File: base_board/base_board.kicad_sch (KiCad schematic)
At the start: 56 parts, among them J1 Conn_ARM_JTAG_SWD_20, SW1 SW_Push, U1 STM32F446ZEJx, U2 IS42S16400J-xT, U3 BMI270, U4 USB_C_Receptacle_USB2.0, U5 10p, U6 10p, U7 LD3985M33R_SOT23, Y1 Crystal_GND24

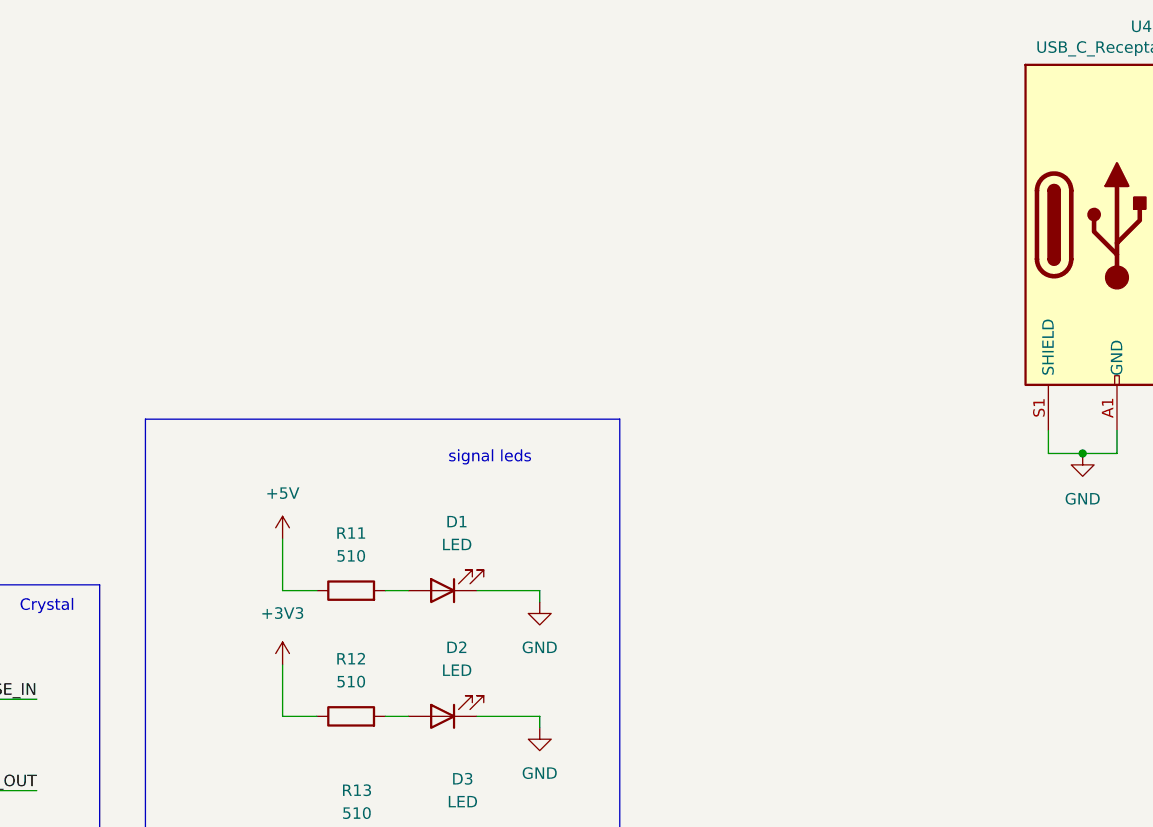
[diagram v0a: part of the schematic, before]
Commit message: [pcb] added onboard uart
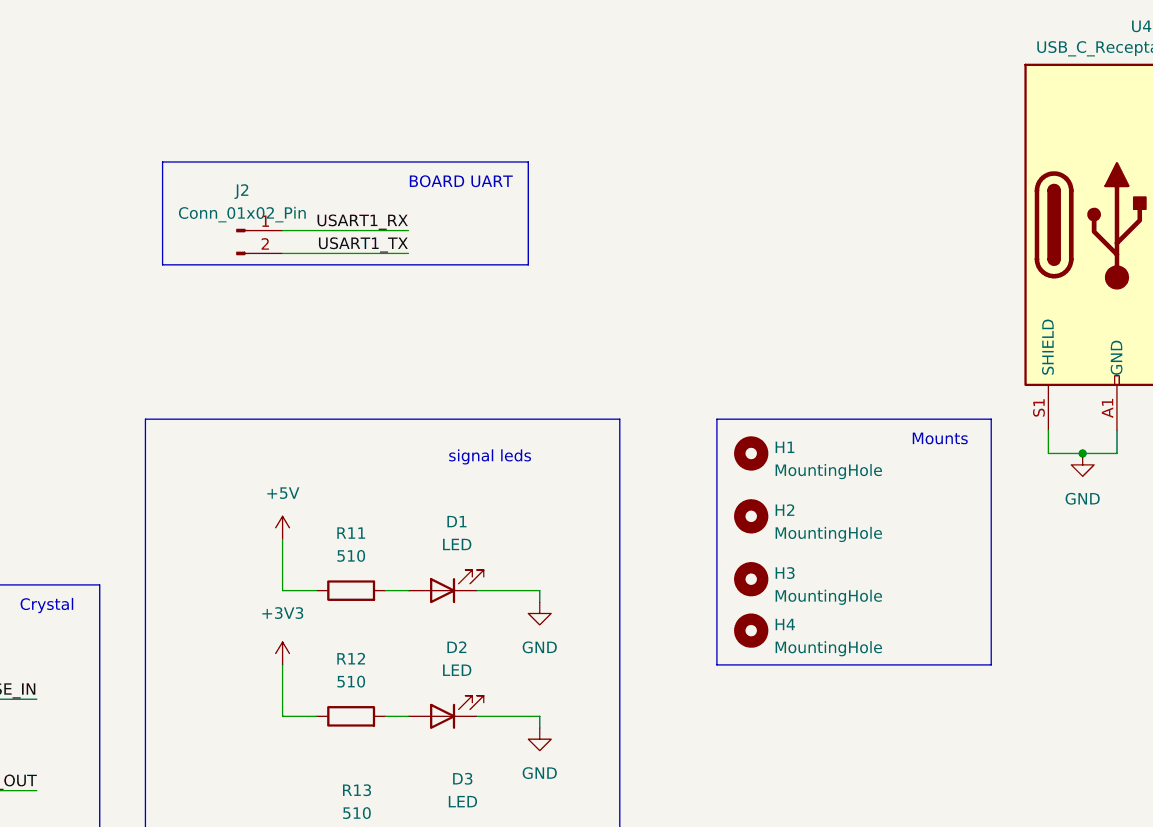
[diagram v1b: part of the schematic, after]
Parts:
- added H1, H2, H3, H4: MountingHole, MountingHole:MountingHole_3.2mm_M3, symbol Mechanical:MountingHole
- added J2: Conn_01x02_Pin, Connector_PinHeader_2.54mm:PinHeader_1x02_P2.54mm_Vertical, symbol Connector:Conn_01x02_Pin
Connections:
- net USART1_RX: now also J2.1 (Pin_1)
- net USART1_TX: now also J2.2 (Pin_2)
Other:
- note added: "BOARD UART"
- note added: "Mounts"
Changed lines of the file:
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@@
+    (stroke (width 0) (type default))
+  )
+  (wire (pts (xy 250.19 206.375) (xy 264.16 206.375))
     (stroke (width 0) (type default))
   )
@@
     (stroke (width 0) (type default))
   )
+  (wire (pts (xy 250.19 203.835) (xy 264.16 203.835))
+    (stroke (width 0) (type default))
+  )
   (wire (pts (xy 257.81 54.61) (xy 275.59 54.61))
     (stroke (width 0) (type default))
@@
     (stroke (width 0) (type default))
   )
+  (rectangle (start 236.855 196.215) (end 277.495 207.645)
+    (stroke (width 0) (type default))
+    (fill (type none))
+  )
+  (rectangle (start 298.45 224.79) (end 328.93 252.095)
+    (stroke (width 0) (type default))
+    (fill (type none))
+  )
   (text "JTAG" (at 86.995 17.78 0)
     (effects (font (size 1.27 1.27)) (justify left bottom))
   )
+  (text "BOARD UART\n" (at 264.16 199.39 0)
+    (effects (font (size 1.27 1.27)) (justify left bottom))
+  )
   (text "Reset circuit" (at 70.485 246.38 0)
     (effects (font (size 1.27 1.27)) (justify left bottom))
@@
     (effects (font (size 1.27 1.27)) (justify left bottom))
   )
+  (text "Mounts\n" (at 320.04 227.965 0)
+    (effects (font (size 1.27 1.27)) (justify left bottom))
+  )
   (text "imu sensor" (at 97.155 107.95 0)
     (effects (font (size 1.27 1.27)) (justify left bottom))
@@
     (effects (font (size 1.27 1.27)) (justify right bottom))
   )
+  (label "USART1_TX" (at 264.16 206.375 180) (fields_autoplaced)
+    (effects (font (size 1.27 1.27)) (justify right bottom))
+  )
   (label "FMC_A8" (at 257.81 82.55 0) (fields_autoplaced)
     (effects (font (size 1.27 1.27)) (justify left bottom))
@@
   (label "PF7" (at 123.19 134.62 0) (fields_autoplaced)
     (effects (font (size 1.27 1.27)) (justify left bottom))
+  )
+  (label "USART1_RX" (at 264.16 203.835 180) (fields_autoplaced)
+    (effects (font (size 1.27 1.27)) (justify right bottom))
   )
   (label "FMC_SDNE1" (at 222.25 88.9 180) (fields_autoplaced)
@@
         (path "/2307506f-1d7e-4fdb-b101-b9905788fe29"
           (reference "J1") (unit 1)
+        )
+      )
+    )
+  )
+  (symbol (lib_id "Mechanical:MountingHole") (at 302.26 248.285 0) (unit 1)
+    (in_bom yes) (on_board yes) (dnp no) (fields_autoplaced)
+    (property "Reference" "H4" (at 304.8 247.65 0)
+      (effects (font (size 1.27 1.27)) (justify left))
+    )
+    (property "Value" "MountingHole" (at 304.8 250.19 0)
+      (effects (font (size 1.27 1.27)) (justify left))
+    )
+    (property "Footprint" "MountingHole:MountingHole_3.2mm_M3" (at 302.26 248.285 0)
+      (effects (font (size 1.27 1.27)) hide)
+    )
+    (property "Datasheet" "~" (at 302.26 248.285 0)
+      (effects (font (size 1.27 1.27)) hide)
+    )
+    (instances
+      (project "base_board"
+        (path "/2307506f-1d7e-4fdb-b101-b9905788fe29"
+          (reference "H4") (unit 1)
         )
       )
@@
     )
   )
+  (symbol (lib_id "Connector:Conn_01x02_Pin") (at 245.11 203.835 0) (unit 1)
+    (in_bom yes) (on_board yes) (dnp no) (fields_autoplaced)
+    (property "Reference" "J2" (at 245.745 199.39 0)
+      (effects (font (size 1.27 1.27)))
+    )
+    (property "Value" "Conn_01x02_Pin" (at 245.745 201.93 0)
+      (effects (font (size 1.27 1.27)))
+    )
+    (property "Footprint" "Connector_PinHeader_2.54mm:PinHeader_1x02_P2.54mm_Vertical" (at 245.11 203.835 0)
+      (effects (font (size 1.27 1.27)) hide)
+    )
+    (property "Datasheet" "~" (at 245.11 203.835 0)
+      (effects (font (size 1.27 1.27)) hide)
+    )
+    (pin "1")
+    (pin "2")
+    (instances
+      (project "base_board"
+        (path "/2307506f-1d7e-4fdb-b101-b9905788fe29"
+          (reference "J2") (unit 1)
+        )
+      )
+    )
+  )
   (symbol (lib_id "power:+3V3") (at 92.075 122.555 0) (unit 1)
     (in_bom yes) (on_board yes) (dnp no) (fields_autoplaced)
@@
         (path "/2307506f-1d7e-4fdb-b101-b9905788fe29"
           (reference "R7") (unit 1)
+        )
+      )
+    )
+  )
+  (symbol (lib_id "Mechanical:MountingHole") (at 302.26 228.6 0) (unit 1)
+    (in_bom yes) (on_board yes) (dnp no) (fields_autoplaced)
+    (property "Reference" "H1" (at 304.8 227.965 0)
+      (effects (font (size 1.27 1.27)) (justify left))
+    )
+    (property "Value" "MountingHole" (at 304.8 230.505 0)
+      (effects (font (size 1.27 1.27)) (justify left))
+    )
+    (property "Footprint" "MountingHole:MountingHole_3.2mm_M3" (at 302.26 228.6 0)
+      (effects (font (size 1.27 1.27)) hide)
+    )
+    (property "Datasheet" "~" (at 302.26 228.6 0)
+      (effects (font (size 1.27 1.27)) hide)
+    )
+    (instances
+      (project "base_board"
+        (path "/2307506f-1d7e-4fdb-b101-b9905788fe29"
+          (reference "H1") (unit 1)
         )
       )
@@
     )
   )
+  (symbol (lib_id "Mechanical:MountingHole") (at 302.26 242.57 0) (unit 1)
+    (in_bom yes) (on_board yes) (dnp no) (fields_autoplaced)
+    (property "Reference" "H3" (at 304.8 241.935 0)
+      (effects (font (size 1.27 1.27)) (justify left))
+    )
+    (property "Value" "MountingHole" (at 304.8 244.475 0)
+      (effects (font (size 1.27 1.27)) (justify left))
+    )
+    (property "Footprint" "MountingHole:MountingHole_3.2mm_M3" (at 302.26 242.57 0)
+      (effects (font (size 1.27 1.27)) hide)
+    )
+    (property "Datasheet" "~" (at 302.26 242.57 0)
+      (effects (font (size 1.27 1.27)) hide)
+    )
+    (instances
+      (project "base_board"
+        (path "/2307506f-1d7e-4fdb-b101-b9905788fe29"
+          (reference "H3") (unit 1)
+        )
+      )
+    )
+  )
   (symbol (lib_id "Device:C") (at 323.85 154.94 0) (unit 1)
     (in_bom yes) (on_board yes) (dnp no) (fields_autoplaced)
@@
         )
       )
+    )
+  )
+  (symbol (lib_id "Mechanical:MountingHole") (at 302.26 235.585 0) (unit 1)
+    (in_bom yes) (on_board yes) (dnp no) (fields_autoplaced)
+    (property "Reference" "H2" (at 304.8 234.95 0)
+      (effects (font (size 1.27 1.27)) (justify left))
+    )
+    (property "Value" "MountingHole" (at 304.8 237.49 0)
+      (effects (font (size 1.27 1.27)) (justify left))
+    )
+    (property "Footprint" "MountingHole:MountingHole_3.2mm_M3" (at 302.26 235.585 0)
+      (effects (font (size 1.27 1.27)) hide)
+    )
+    (property "Datasheet" "~" (at 302.26 235.585 0)
+      (effects (font (size 1.27 1.27)) hide)
+    )
+    (instances
+      (project "base_board"
+        (path "/2307506f-1d7e-4fdb-b101-b9905788fe29"
+          (reference "H2") (unit 1)
+        )
+      )

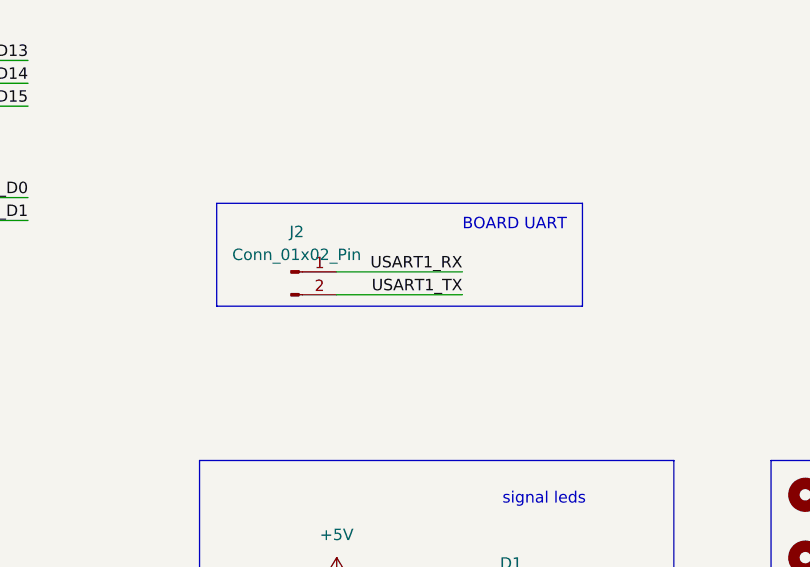
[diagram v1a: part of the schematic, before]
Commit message: [pcb] added gnd+3v3 for uart socket
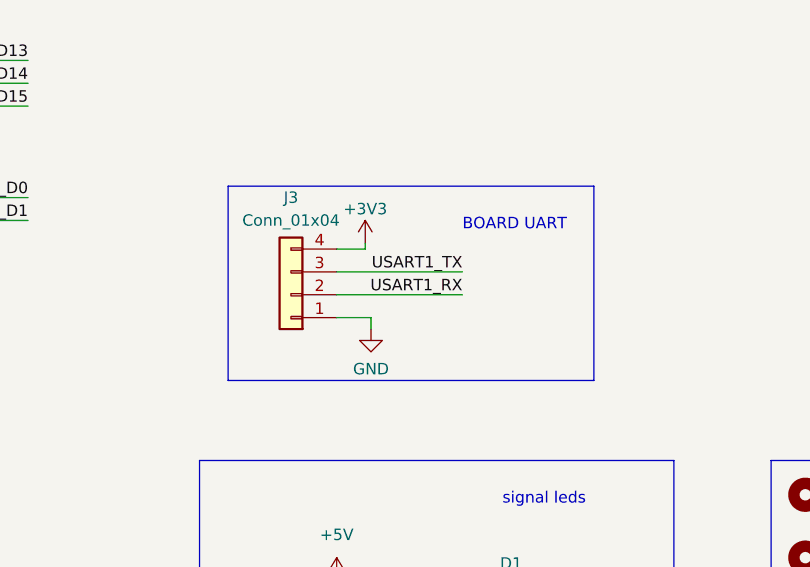
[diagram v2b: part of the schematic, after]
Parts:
- removed J2: Conn_01x02_Pin, Connector_PinHeader_2.54mm:PinHeader_1x02_P2.54mm_Vertical, symbol Connector:Conn_01x02_Pin
- added J3: Conn_01x04, Connector_PinHeader_2.54mm:PinHeader_1x04_P2.54mm_Vertical, symbol Connector_Generic:Conn_01x04
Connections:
- net +3V3: now also J3.4 (Pin_4)
- net GND: now also J3.1 (Pin_1)
- net USART1_RX: now also J3.2 (Pin_2)
- net USART1_TX: now also J3.3 (Pin_3)
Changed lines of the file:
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@@
+    (stroke (width 0) (type default))
+  )
+  (wire (pts (xy 253.365 200.66) (xy 253.365 201.295))
     (stroke (width 0) (type default))
   )
@@
     (stroke (width 0) (type default))
   )
+  (wire (pts (xy 253.365 201.295) (xy 250.19 201.295))
+    (stroke (width 0) (type default))
+  )
   (polyline (pts (xy 234.95 280.035) (xy 287.655 280.035))
     (stroke (width 0) (type default))
@@
     (stroke (width 0) (type default))
   )
+  (wire (pts (xy 254 208.915) (xy 250.19 208.915))
+    (stroke (width 0) (type default))
+  )
   (wire (pts (xy 123.825 73.66) (xy 138.43 73.66))
     (stroke (width 0) (type default))
@@
     (stroke (width 0) (type default))
   )
+  (wire (pts (xy 254 210.185) (xy 254 208.915))
+    (stroke (width 0) (type default))
+  )
   (wire (pts (xy 300.99 54.61) (xy 311.15 54.61))
     (stroke (width 0) (type default))
@@
     (stroke (width 0) (type default))
   )
-  (rectangle (start 236.855 196.215) (end 277.495 207.645)
+  (rectangle (start 238.125 194.31) (end 278.765 215.9)
     (stroke (width 0) (type default))
     (fill (type none))
@@
     (effects (font (size 1.27 1.27)) (justify right bottom))
   )
-  (label "USART1_TX" (at 264.16 206.375 180) (fields_autoplaced)
+  (label "USART1_TX" (at 264.16 203.835 180) (fields_autoplaced)
     (effects (font (size 1.27 1.27)) (justify right bottom))
   )
@@
     (effects (font (size 1.27 1.27)) (justify left bottom))
   )
-  (label "USART1_RX" (at 264.16 203.835 180) (fields_autoplaced)
+  (label "USART1_RX" (at 264.16 206.375 180) (fields_autoplaced)
     (effects (font (size 1.27 1.27)) (justify right bottom))
   )
@@
         (path "/2307506f-1d7e-4fdb-b101-b9905788fe29"
           (reference "R1") (unit 1)
+        )
+      )
+    )
+  )
+  (symbol (lib_name "+3V3_8") (lib_id "power:+3V3") (at 253.365 200.66 0) (unit 1)
+    (in_bom yes) (on_board yes) (dnp no) (fields_autoplaced)
+    (property "Reference" "#PWR011" (at 253.365 204.47 0)
+      (effects (font (size 1.27 1.27)) hide)
+    )
+    (property "Value" "+3V3" (at 253.365 196.85 0)
+      (effects (font (size 1.27 1.27)))
+    )
+    (property "Footprint" "" (at 253.365 200.66 0)
+      (effects (font (size 1.27 1.27)) hide)
+    )
+    (property "Datasheet" "" (at 253.365 200.66 0)
+      (effects (font (size 1.27 1.27)) hide)
+    )
+    (pin "1")
+    (instances
+      (project "base_board"
+        (path "/2307506f-1d7e-4fdb-b101-b9905788fe29"
+          (reference "#PWR011") (unit 1)
         )
       )
@@
     )
   )
-  (symbol (lib_id "Connector:Conn_01x02_Pin") (at 245.11 203.835 0) (unit 1)
-    (in_bom yes) (on_board yes) (dnp no) (fields_autoplaced)
-    (property "Reference" "J2" (at 245.745 199.39 0)
-      (effects (font (size 1.27 1.27)))
-    )
-    (property "Value" "Conn_01x02_Pin" (at 245.745 201.93 0)
-      (effects (font (size 1.27 1.27)))
-    )
-    (property "Footprint" "Connector_PinHeader_2.54mm:PinHeader_1x02_P2.54mm_Vertical" (at 245.11 203.835 0)
-      (effects (font (size 1.27 1.27)) hide)
-    )
-    (property "Datasheet" "~" (at 245.11 203.835 0)
-      (effects (font (size 1.27 1.27)) hide)
-    )
-    (pin "1")
-    (pin "2")
-    (instances
-      (project "base_board"
-        (path "/2307506f-1d7e-4fdb-b101-b9905788fe29"
-          (reference "J2") (unit 1)
-        )
-      )
-    )
-  )
   (symbol (lib_id "power:+3V3") (at 92.075 122.555 0) (unit 1)
     (in_bom yes) (on_board yes) (dnp no) (fields_autoplaced)
@@
         (path "/2307506f-1d7e-4fdb-b101-b9905788fe29"
           (reference "#PWR0123") (unit 1)
+        )
+      )
+    )
+  )
+  (symbol (lib_name "GND_2") (lib_id "power:GND") (at 254 210.185 0) (unit 1)
+    (in_bom yes) (on_board yes) (dnp no) (fields_autoplaced)
+    (property "Reference" "#PWR010" (at 254 216.535 0)
+      (effects (font (size 1.27 1.27)) hide)
+    )
+    (property "Value" "GND" (at 254 214.63 0)
+      (effects (font (size 1.27 1.27)))
+    )
+    (property "Footprint" "" (at 254 210.185 0)
+      (effects (font (size 1.27 1.27)) hide)
+    )
+    (property "Datasheet" "" (at 254 210.185 0)
+      (effects (font (size 1.27 1.27)) hide)
+    )
+    (pin "1")
+    (instances
+      (project "base_board"
+        (path "/2307506f-1d7e-4fdb-b101-b9905788fe29"
+          (reference "#PWR010") (unit 1)
         )
       )
@@
         )
       )
+    )
+  )
+  (symbol (lib_id "Connector_Generic:Conn_01x04") (at 245.11 206.375 180) (unit 1)
+    (in_bom yes) (on_board yes) (dnp no) (fields_autoplaced)
+    (property "Reference" "J3" (at 245.11 195.58 0)
+      (effects (font (size 1.27 1.27)))
+    )
+    (property "Value" "Conn_01x04" (at 245.11 198.12 0)
+      (effects (font (size 1.27 1.27)))
+    )
+    (property "Footprint" "Connector_PinHeader_2.54mm:PinHeader_1x04_P2.54mm_Vertical" (at 245.11 206.375 0)
+      (effects (font (size 1.27 1.27)) hide)
+    )
+    (property "Datasheet" "~" (at 245.11 206.375 0)
+      (effects (font (size 1.27 1.27)) hide)
+    )
+    (pin "1")
+    (pin "2")
+    (pin "3")
+    (pin "4")
+    (instances
+      (project "base_board"
+        (path "/2307506f-1d7e-4fdb-b101-b9905788fe29"
+          (reference "J3") (unit 1)
+        )
+      )
